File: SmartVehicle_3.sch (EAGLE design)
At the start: 129 parts, among them IC1 MPU6050, IC3 ESP8266EX, IC4 24AA32ASN, IC5 TPS77001, IC6 7805T, IC8 TPS77001, J1 U.FL, J3 U.FL, J4 78646-3001, K10 G6A-234P, K6 G6A-234P, K7 G6A-234P, K8 G6A-234P, K9 G6A-234P, Q1 IRF520, Q2 ABM8-26MHz, T10 2N7002, T6 2N7002, T7 2N7002, T8 2N7002, T9 2N7002, U2 MPR121QR2, U3 NEO-6M-GPS, U4 SIM800L, X1 22-23-2021, X10 sign, X11 sign, X12 sign, X8 sign, X9 sign

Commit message: update menambahkan Pin dang menghilangkan Gyro
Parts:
- removed C10, C11, C13: 0.1uF/16V, rcl:C-EUC0603
- removed C12: 2200pF, rcl:C-EUC0603
- removed C31: 4.7uF/16V, rcl:C-EUC0603
- removed C32: 10uF, rcl:C-EUC0603
- removed C33: 0.1uF, rcl:C-EUC0603
- removed IC1: MPU6050, mpu6050:MPU6050
- removed IC5: TPS77001, texas:TPS77001
- removed R2, R7: 4.7K 1%, resistor:R-US_R0603
- removed V+5, V-5: PTR1TP08R, testpad:PTR1TP08R
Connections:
- removed net N$7: C11.1, IC1G$1.REGOUT
- removed net N$8: C12.2, IC1G$1.CPOUT
- net +3V3: no longer C10.2, C13.2, C32.2, C33.2, IC1G$1.VDD, IC1G$1.VLOGIC, IC5.OUT, R2.1, R7.1
- net +5V: no longer C31.2, IC5.!EN, IC5.IN
- net GND: no longer C10.1, C11.2, C12.1, C13.1, C31.1, C32.1, C33.1, IC1G$1.CLKIN, IC1G$1.FSYNC, IC1G$1.GND, IC1G$1.GND@1, IC5.GND, V+5.TP, V-5.TP
- net IO4: no longer IC1G$1.SDA, R7.2
- net IO5: no longer IC1G$1.SCL, R2.2

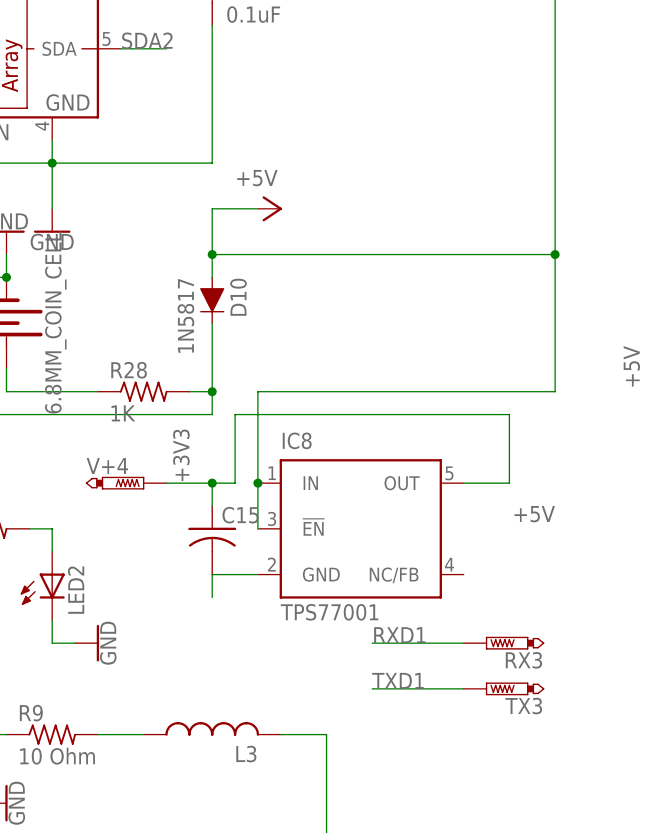
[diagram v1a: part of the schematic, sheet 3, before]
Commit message: menambahkan battery dan fix GPS
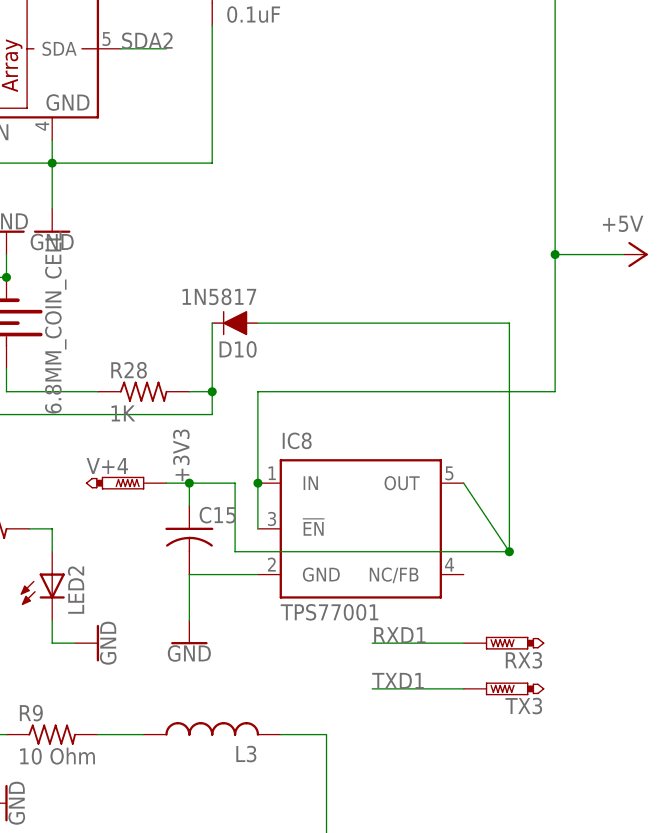
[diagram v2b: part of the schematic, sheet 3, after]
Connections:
- removed net N$56: K72.O, X9-2.S
- removed net N$59: K73.S, X9-1.S
- new net N$32: K72.S, X9-2.S
- net +12V: now also X1-1.S; no longer X1-2.S
- net +3V3: now also D10.A
- net +5V: no longer D10.A
- net GND: now also X1-2.S; no longer X1-1.S
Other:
- moved on the sheet: C15, D10, X1-1, X1-2, X9-1, X9-2
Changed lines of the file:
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@@
 <setting verticaltext="up"/>
 </settings>
-<grid distance="0.1" unitdist="inch" unit="inch" style="lines" multiple="1" display="no" altdistance="0.01" altunitdist="inch" altunit="inch"/>
+<grid distance="0.1" unitdist="inch" unit="inch" style="lines" multiple="1" display="yes" altdistance="0.01" altunitdist="inch" altunit="inch"/>
 <layers>
 <layer number="1" name="Top" color="4" fill="1" visible="no" active="no"/>
@@
 <part name="+3V9" library="supply1" deviceset="+3V3" device=""/>
 <part name="+3V10" library="supply1" deviceset="+3V3" device=""/>
+<part name="GND2" library="SparkFun-PowerSymbols" deviceset="GND" device=""/>
 </parts>
 <sheets>
@@
 <instances>
 <instance part="U3" gate="G$1" x="93.98" y="76.2"/>
-<instance part="D10" gate="G$1" x="147.32" y="106.68" rot="R270"/>
+<instance part="D10" gate="G$1" x="149.86" y="104.14" rot="R180"/>
 <instance part="IC4" gate="G$1" x="121.92" y="134.62"/>
 <instance part="C14" gate="G$1" x="147.32" y="139.7"/>
@@
 <instance part="IC8" gate="G$1" x="162.56" y="81.28"/>
 <instance part="V+4" gate="G$1" x="139.7" y="86.36" rot="R270"/>
-<instance part="C15" gate="G$1" x="147.32" y="81.28"/>
+<instance part="C15" gate="G$1" x="144.78" y="81.28"/>
 <instance part="GND35" gate="1" x="124.46" y="114.3" rot="R180"/>
 <instance part="RX3" gate="G$1" x="177.8" y="68.58" rot="R90"/>
@@
 <instance part="R28" gate="G$1" x="139.7" y="96.52"/>
 <instance part="FRAME3" gate="G$1" x="0" y="0"/>
-<instance part="P+8" gate="1" x="154.94" y="116.84" rot="R270"/>
+<instance part="P+8" gate="1" x="195.58" y="111.76" rot="R270"/>
 <instance part="+3V9" gate="G$1" x="154.94" y="149.86" rot="R270"/>
 <instance part="+3V10" gate="G$1" x="116.84" y="114.3"/>
+<instance part="GND2" gate="1" x="144.78" y="68.58"/>
 </instances>
 <busses>
@@
 <segment>
 <pinref part="V+4" gate="G$1" pin="TP"/>
-<wire x1="142.24" y1="86.36" x2="147.32" y2="86.36" width="0.1524" layer="91"/>
+<wire x1="142.24" y1="86.36" x2="144.78" y2="86.36" width="0.1524" layer="91"/>
 <pinref part="C15" gate="G$1" pin="1"/>
-<wire x1="147.32" y1="86.36" x2="149.86" y2="86.36" width="0.1524" layer="91"/>
-<wire x1="147.32" y1="86.36" x2="147.32" y2="83.82" width="0.1524" layer="91"/>
-<junction x="147.32" y="86.36"/>
+<wire x1="144.78" y1="86.36" x2="149.86" y2="86.36" width="0.1524" layer="91"/>
+<wire x1="144.78" y1="86.36" x2="144.78" y2="83.82" width="0.1524" layer="91"/>
+<junction x="144.78" y="86.36"/>
 <label x="144.78" y="86.36" size="1.778" layer="95" rot="R90"/>
-<wire x1="149.86" y1="86.36" x2="149.86" y2="93.98" width="0.1524" layer="91"/>
-<wire x1="149.86" y1="93.98" x2="180.34" y2="93.98" width="0.1524" layer="91"/>
-<wire x1="180.34" y1="93.98" x2="180.34" y2="86.36" width="0.1524" layer="91"/>
+<wire x1="149.86" y1="86.36" x2="149.86" y2="78.74" width="0.1524" layer="91"/>
+<wire x1="149.86" y1="78.74" x2="180.34" y2="78.74" width="0.1524" layer="91"/>
 <pinref part="IC8" gate="G$1" pin="OUT"/>
-<wire x1="180.34" y1="86.36" x2="175.26" y2="86.36" width="0.1524" layer="91"/>
+<wire x1="180.34" y1="78.74" x2="175.26" y2="86.36" width="0.1524" layer="91"/>
+<pinref part="D10" gate="G$1" pin="A"/>
+<wire x1="152.4" y1="104.14" x2="180.34" y2="104.14" width="0.1524" layer="91"/>
+<wire x1="180.34" y1="104.14" x2="180.34" y2="78.74" width="0.1524" layer="91"/>
+<junction x="180.34" y="78.74"/>
 </segment>
 <segment>
@@
 <segment>
 <pinref part="IC8" gate="G$1" pin="GND"/>
-<wire x1="147.32" y1="76.2" x2="152.4" y2="76.2" width="0.1524" layer="91"/>
+<wire x1="144.78" y1="76.2" x2="152.4" y2="76.2" width="0.1524" layer="91"/>
 <pinref part="C15" gate="G$1" pin="2"/>
-<wire x1="147.32" y1="76.2" x2="147.32" y2="73.66" width="0.1524" layer="91"/>
+<wire x1="144.78" y1="76.2" x2="144.78" y2="71.12" width="0.1524" layer="91"/>
+<pinref part="GND2" gate="1" pin="GND"/>
 </segment>
 </net>
@@
 <net name="+5V" class="0">
 <segment>
-<pinref part="D10" gate="G$1" pin="A"/>
-<wire x1="147.32" y1="109.22" x2="147.32" y2="111.76" width="0.1524" layer="91"/>
 <pinref part="C14" gate="G$1" pin="1"/>
-<label x="185.42" y="83.82" size="1.778" layer="95" rot="R180"/>
 <wire x1="147.32" y1="147.32" x2="147.32" y2="144.78" width="0.1524" layer="91"/>
 <wire x1="185.42" y1="96.52" x2="185.42" y2="111.76" width="0.1524" layer="91"/>
 <wire x1="185.42" y1="111.76" x2="185.42" y2="147.32" width="0.1524" layer="91"/>
 <wire x1="185.42" y1="147.32" x2="147.32" y2="147.32" width="0.1524" layer="91"/>
-<wire x1="147.32" y1="111.76" x2="185.42" y2="111.76" width="0.1524" layer="91"/>
 <junction x="185.42" y="111.76"/>
 <pinref part="IC8" gate="G$1" pin="IN"/>
@@
 <wire x1="152.4" y1="81.28" x2="152.4" y2="86.36" width="0.1524" layer="91"/>
 <junction x="152.4" y="86.36"/>
-<label x="193.04" y="101.6" size="1.778" layer="95" rot="R270"/>
 <pinref part="P+8" gate="1" pin="+5V"/>
-<wire x1="147.32" y1="111.76" x2="147.32" y2="116.84" width="0.1524" layer="91"/>
-<wire x1="147.32" y1="116.84" x2="152.4" y2="116.84" width="0.1524" layer="91"/>
-<junction x="147.32" y="111.76"/>
+<wire x1="193.04" y1="111.76" x2="185.42" y2="111.76" width="0.1524" layer="91"/>
 </segment>
 </net>
@@
 <instance part="K7" gate="2" x="63.5" y="83.82"/>
 <instance part="K7" gate="3" x="63.5" y="68.58"/>
-<instance part="X9" gate="-1" x="76.2" y="73.66"/>
-<instance part="X9" gate="-2" x="76.2" y="88.9"/>
+<instance part="X9" gate="-1" x="76.2" y="81.28"/>
+<instance part="X9" gate="-2" x="76.2" y="93.98"/>
 <instance part="R30" gate="G$1" x="114.3" y="127"/>
 <instance part="R31" gate="G$1" x="124.46" y="119.38" rot="R90"/>
@@
 </segment>
 </net>
-<net name="N$56" class="0">
-<segment>
-<pinref part="K7" gate="2" pin="O"/>
-<pinref part="X9" gate="-2" pin="S"/>
-<wire x1="73.66" y1="88.9" x2="68.58" y2="88.9" width="0.1524" layer="91"/>
-</segment>
-</net>
-<net name="N$59" class="0">
-<segment>
-<pinref part="K7" gate="3" pin="S"/>
-<wire x1="58.42" y1="73.66" x2="55.88" y2="73.66" width="0.1524" layer="91"/>
-<wire x1="55.88" y1="73.66" x2="55.88" y2="78.74" width="0.1524" layer="91"/>
-<wire x1="55.88" y1="78.74" x2="71.12" y2="78.74" width="0.1524" layer="91"/>
-<wire x1="71.12" y1="78.74" x2="71.12" y2="73.66" width="0.1524" layer="91"/>
-<pinref part="X9" gate="-1" pin="S"/>
-<wire x1="71.12" y1="73.66" x2="73.66" y2="73.66" width="0.1524" layer="91"/>
-</segment>
-</net>
 <net name="N$60" class="0">
 <segment>
@@
 <pinref part="K7" gate="2" pin="P"/>
 <wire x1="53.34" y1="81.28" x2="63.5" y2="81.28" width="0.1524" layer="91"/>
+</segment>
+</net>
+<net name="N$32" class="0">
+<segment>
+<pinref part="K7" gate="2" pin="S"/>
+<wire x1="58.42" y1="88.9" x2="55.88" y2="88.9" width="0.1524" layer="91"/>
+<wire x1="55.88" y1="88.9" x2="55.88" y2="93.98" width="0.1524" layer="91"/>
+<wire x1="55.88" y1="93.98" x2="73.66" y2="93.98" width="0.1524" layer="91"/>
+<pinref part="X9" gate="-2" pin="S"/>
 </segment>
 </net>
@@
 <instance part="D2" gate="G$1" x="40.64" y="152.4"/>
 <instance part="FRAME4" gate="G$1" x="0" y="2.54"/>
-<instance part="X1" gate="-1" x="27.94" y="134.62" rot="R180"/>
-<instance part="X1" gate="-2" x="27.94" y="152.4" rot="R180"/>
+<instance part="X1" gate="-1" x="30.48" y="152.4" rot="R180"/>
+<instance part="X1" gate="-2" x="33.02" y="134.62" rot="R180"/>
 </instances>
 <busses>
@@
 <wire x1="53.34" y1="134.62" x2="73.66" y2="134.62" width="0.1524" layer="91"/>
 <junction x="73.66" y="134.62"/>
-<wire x1="53.34" y1="134.62" x2="30.48" y2="134.62" width="0.1524" layer="91"/>
-<pinref part="X1" gate="-1" pin="S"/>
-<junction x="30.48" y="134.62"/>
-<junction x="53.34" y="134.62"/>
+<pinref part="X1" gate="-2" pin="S"/>
+<wire x1="53.34" y1="134.62" x2="35.56" y2="134.62" width="0.1524" layer="91"/>
 </segment>
 </net>
@@
 <pinref part="P+2" gate="1" pin="+12V"/>
 <wire x1="33.02" y1="152.4" x2="33.02" y2="154.94" width="0.1524" layer="91"/>
-<wire x1="33.02" y1="152.4" x2="30.48" y2="152.4" width="0.1524" layer="91"/>
+<pinref part="D2" gate="G$1" pin="A"/>
+<pinref part="X1" gate="-1" pin="S"/>
 <junction x="33.02" y="152.4"/>
-<pinref part="D2" gate="G$1" pin="A"/>
-<pinref part="X1" gate="-2" pin="S"/>
-</segment>
-</net>
+</segment>
+</net>
